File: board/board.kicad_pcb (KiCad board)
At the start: 4 copper layers, 21 x 13 mm, 4 parts, among them J1 0xx_LED, J2 0xx_LED

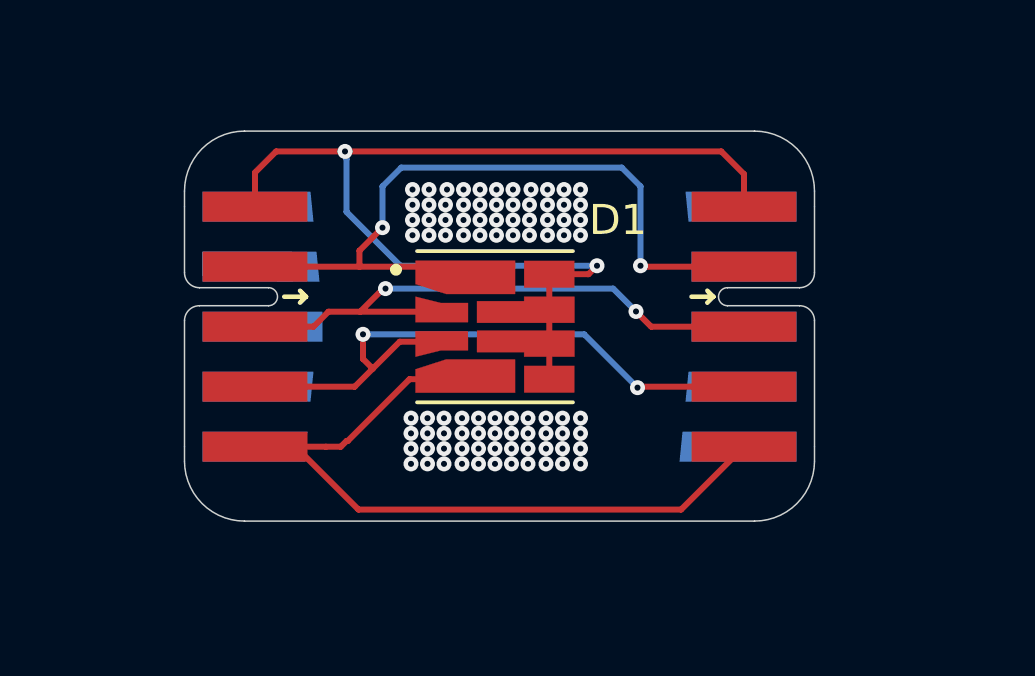
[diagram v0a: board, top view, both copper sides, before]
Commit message: Update surface and connected vias | Change common ground to common anode
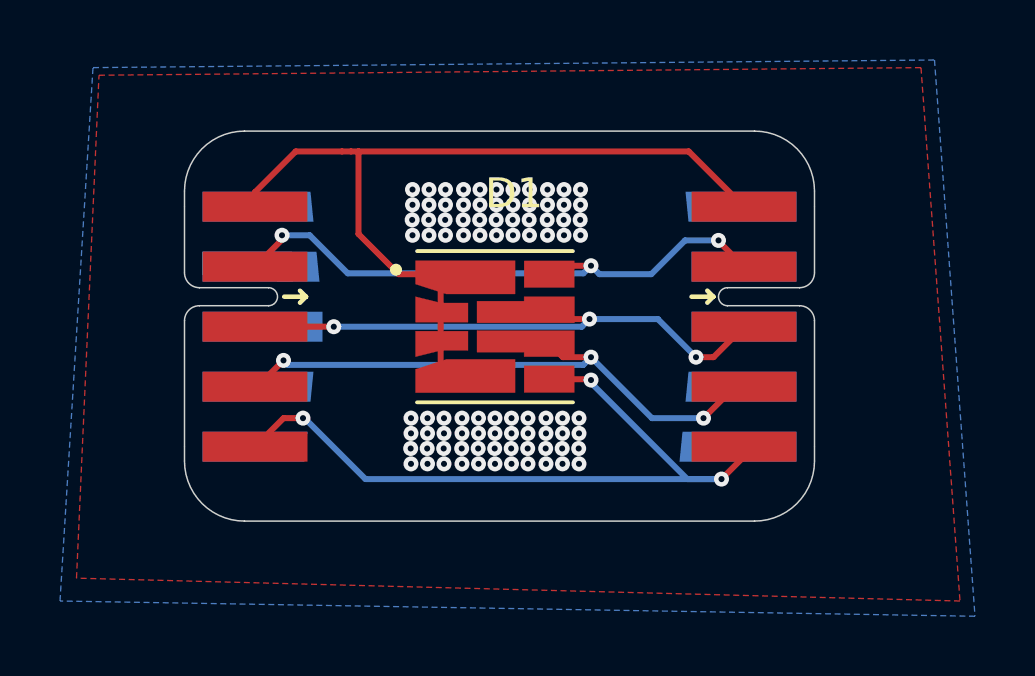
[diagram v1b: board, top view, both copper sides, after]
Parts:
- moved LOGO1 3.06 mm to (150.3, 96.0)
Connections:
- D1 pad 2: Net-(D1-Pad2) -> Net-(D1-Pad1)
- D1 pad 3: Net-(D1-Pad3) -> Net-(D1-Pad1)
- D1 pad 4: Net-(D1-Pad4) -> Net-(D1-Pad1)
- D1 pad 5: Net-(D1-Pad7) -> Net-(D1-Pad5)
- D1 pad 6: Net-(D1-Pad7) -> Net-(D1-Pad6)
- D1 pad 8: Net-(D1-Pad7) -> Net-(J2-Pad2)
- J1 pad 1: Net-(D1-Pad7) -> Net-(D1-Pad1)
- J1 pad 2: Net-(D1-Pad1) -> Net-(J2-Pad2)
- J1 pad 3: Net-(D1-Pad2) -> Net-(D1-Pad7)
- J1 pad 4: Net-(D1-Pad3) -> Net-(D1-Pad6)
- J1 pad 5: Net-(D1-Pad4) -> Net-(D1-Pad5)
- J2 pad 1: Net-(D1-Pad7) -> Net-(D1-Pad1)
- J2 pad 2: Net-(D1-Pad1) -> Net-(J2-Pad2)
- J2 pad 3: Net-(D1-Pad2) -> Net-(D1-Pad7)
- J2 pad 4: Net-(D1-Pad3) -> Net-(D1-Pad6)
- J2 pad 5: Net-(D1-Pad4) -> Net-(D1-Pad5)
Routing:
- net Net-(D1-Pad5): track 0.00 -> 25.4 mm, vias 0 -> 3
- net Net-(D1-Pad4): track 25.2 -> 0.00 mm
- net Net-(D1-Pad3): track 21.5 -> 0.00 mm, vias 2 -> 0
- net Net-(D1-Pad2): track 20.0 -> 0.00 mm, vias 2 -> 0
- net Net-(J2-Pad2): track 0.00 -> 19.9 mm, vias 0 -> 3
- net Net-(D1-Pad6): track 0.00 -> 19.7 mm, vias 0 -> 3
- net Net-(D1-Pad7): track 35.5 -> 18.8 mm, vias 2 -> 3
- net Net-(D1-Pad1): track 24.5 -> 28.0 mm, vias 2 -> 88
- net (no net): vias 88 -> 0
- added copper zone on B.Cu, net (none)
- added copper zone on F.Cu, net Net-(D1-Pad1)
- added copper zone on In1.Cu, net Net-(D1-Pad1)
- added copper zone on In2.Cu, net Net-(D1-Pad1)
- removed copper zone on In1.Cu, net (none)
- removed copper zone on In2.Cu, net (none)

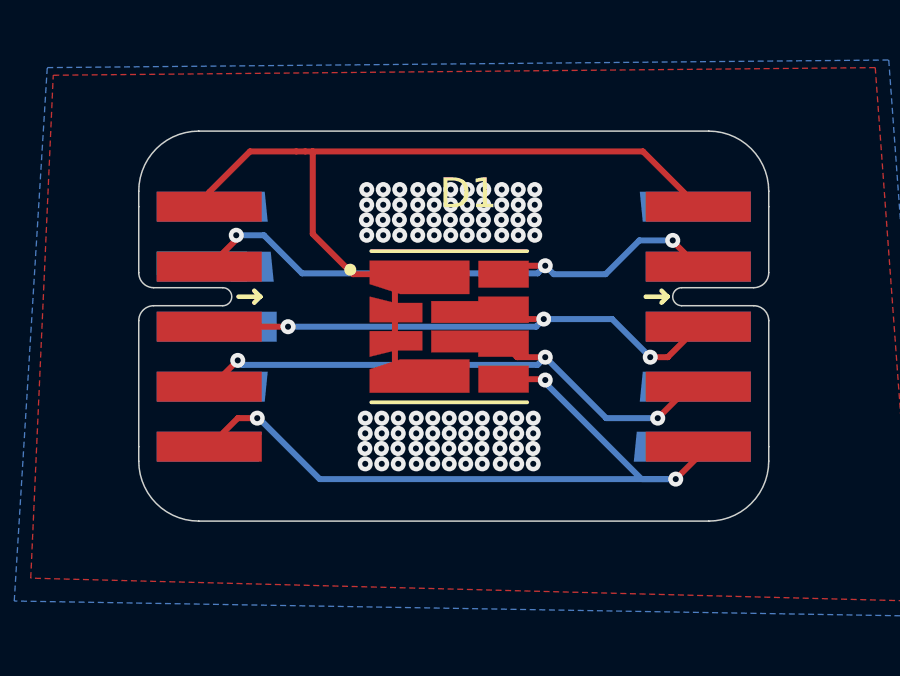
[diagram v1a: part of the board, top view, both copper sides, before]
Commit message: Update Layout | Remove DRC Errors | Connected unused Edgy Pins
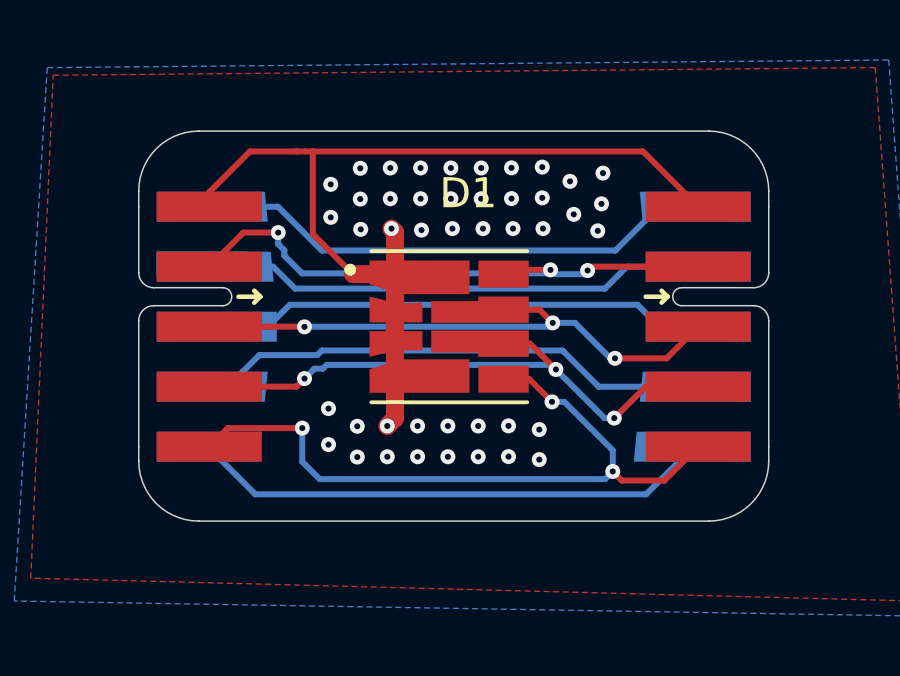
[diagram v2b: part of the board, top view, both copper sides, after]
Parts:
- J1, J2: value 0xx_LED -> 023_LED
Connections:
- J1 pad 10: (no net) -> Net-(J1-Pad10)
- J1 pad 6: (no net) -> Net-(J1-Pad6)
- J1 pad 7: (no net) -> Net-(J1-Pad7)
- J1 pad 8: (no net) -> Net-(J1-Pad8)
- J1 pad 9: (no net) -> Net-(J1-Pad9)
- J2 pad 10: (no net) -> Net-(J1-Pad10)
- J2 pad 6: (no net) -> Net-(J1-Pad6)
- J2 pad 7: (no net) -> Net-(J1-Pad7)
- J2 pad 8: (no net) -> Net-(J1-Pad8)
- J2 pad 9: (no net) -> Net-(J1-Pad9)
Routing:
- net Net-(J1-Pad10): track 0.00 -> 17.5 mm
- net Net-(J1-Pad6): track 0.00 -> 17.4 mm
- net Net-(J1-Pad9): track 0.00 -> 17.2 mm
- net Net-(J1-Pad7): track 0.00 -> 17.2 mm
- net Net-(J1-Pad8): track 0.00 -> 16.7 mm
- net Net-(D1-Pad1): track 28.0 -> 30.9 mm, vias 88 -> 44
- net Net-(D1-Pad5): track 25.4 -> 23.9 mm
- added copper zone on B.Cu, net Net-(D1-Pad1)
- removed copper zone on B.Cu, net (none)

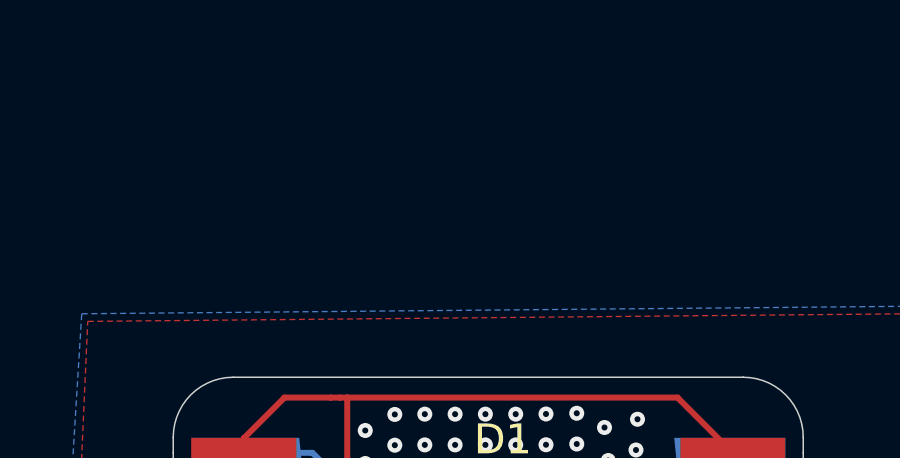
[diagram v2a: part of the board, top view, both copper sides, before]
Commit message: Change edgy connector back to GPIO | Began adding Resistor to specific voltage
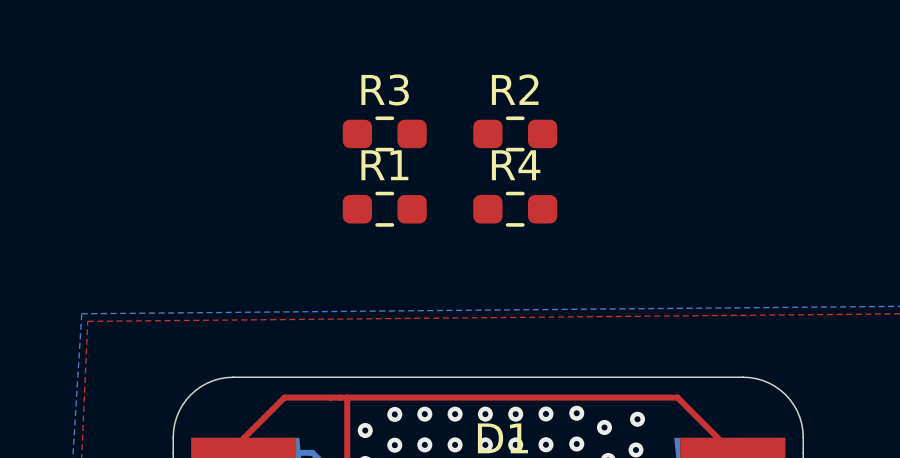
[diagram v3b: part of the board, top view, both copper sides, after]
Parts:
- added R1: R, Resistor_SMD:R_0603_1608Metric_Pad0.98x0.95mm_HandSolder, F.Cu at (147.1, 84.4)
- added R2: R, Resistor_SMD:R_0603_1608Metric_Pad0.98x0.95mm_HandSolder, F.Cu at (151.4, 81.9)
- added R3: R, Resistor_SMD:R_0603_1608Metric_Pad0.98x0.95mm_HandSolder, F.Cu at (147.1, 81.9)
- added R4: R, Resistor_SMD:R_0603_1608Metric_Pad0.98x0.95mm_HandSolder, F.Cu at (151.4, 84.4)
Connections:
- D1 pad 2: Net-(D1-Pad1) -> Net-(D1-Pad2)
- D1 pad 3: Net-(D1-Pad1) -> Net-(D1-Pad3)
- D1 pad 4: Net-(D1-Pad1) -> Net-(D1-Pad4)
- J1 pad 1: Net-(D1-Pad1) -> Net-(J1-Pad1)
- J2 pad 1: Net-(D1-Pad1) -> Net-(J1-Pad1)
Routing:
- net Net-(J1-Pad1): track 0.00 -> 30.9 mm
- net Net-(D1-Pad1): track 30.9 -> 0.00 mm

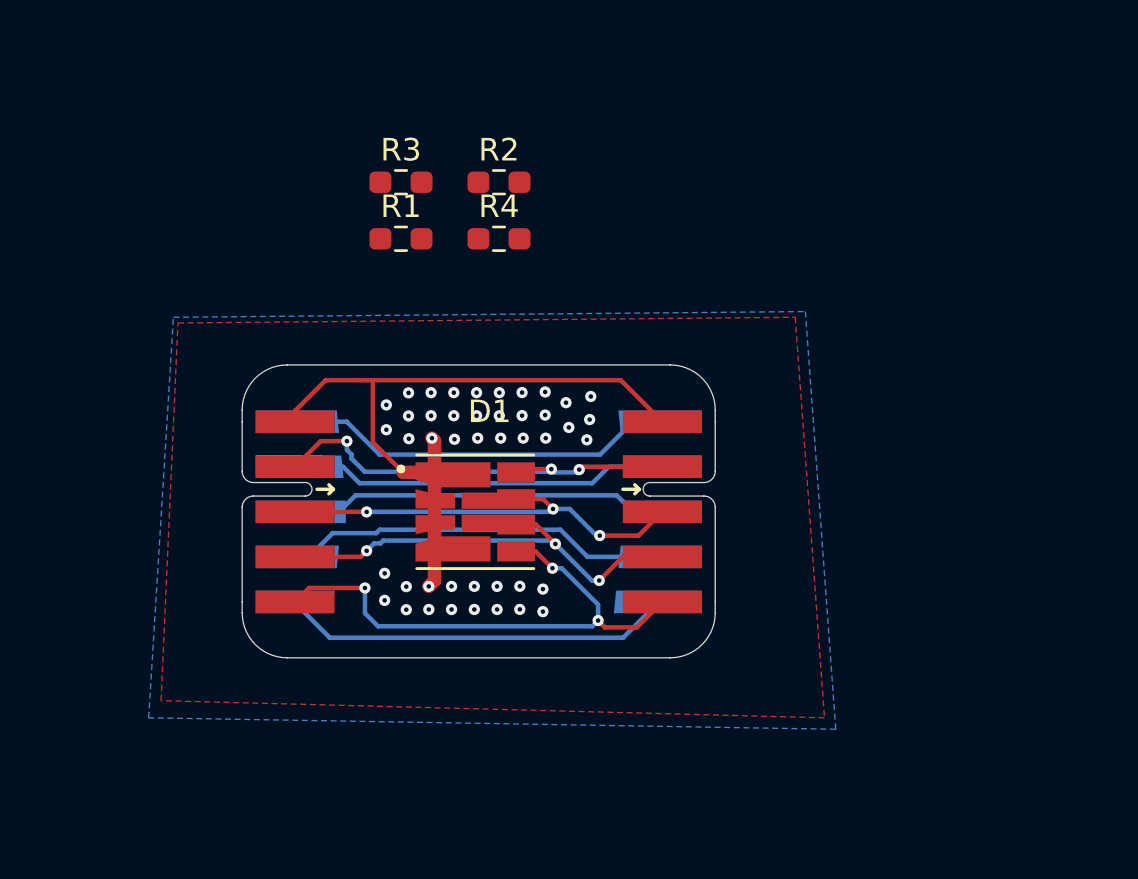
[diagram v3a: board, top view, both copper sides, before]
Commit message: Increase PCB size | Update Design
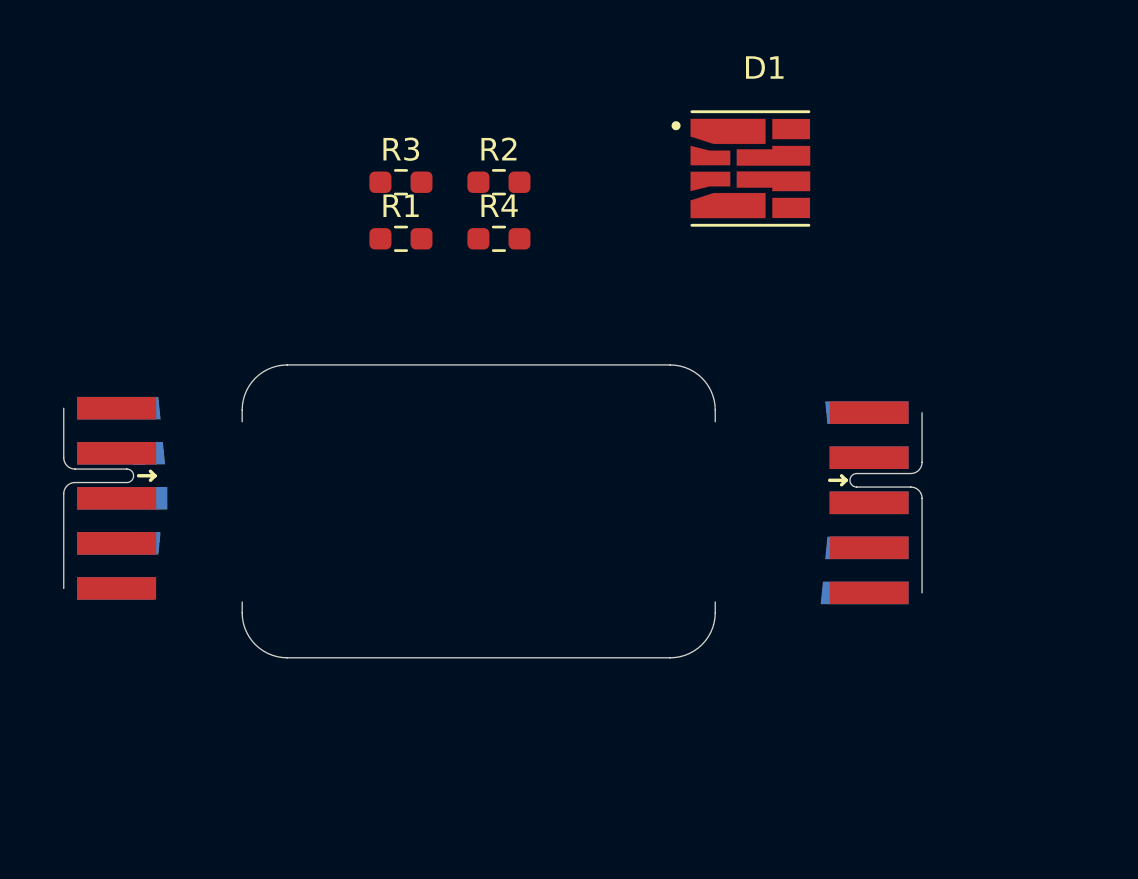
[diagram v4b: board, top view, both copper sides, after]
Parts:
- moved D1 19.5 mm to (162.6, 81.3)
- moved LOGO1 13.5 mm to (147.3, 109.2)
- moved J2 9.19 mm to (170.2, 96.1)
- moved J1 7.94 mm to (132.1, 95.9)
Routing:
- net Net-(J1-Pad1): track 30.9 -> 0.00 mm
- net Net-(D1-Pad5): track 23.9 -> 0.00 mm, vias 3 -> 0
- net Net-(D1-Pad6): track 19.9 -> 0.00 mm, vias 3 -> 0
- net Net-(D1-Pad8): track 19.5 -> 0.00 mm, vias 3 -> 0
- net Net-(D1-Pad7): track 19.1 -> 0.00 mm, vias 3 -> 0
- net Net-(J1-Pad10): track 17.5 -> 0.00 mm
- net Net-(J1-Pad6): track 17.4 -> 0.00 mm
- net Net-(J1-Pad9): track 17.2 -> 0.00 mm
- net Net-(J1-Pad7): track 17.2 -> 0.00 mm
- net Net-(J1-Pad8): track 16.7 -> 0.00 mm
- net Net-(D1-Pad1): vias 44 -> 0
- removed copper zone on B.Cu, net Net-(D1-Pad1)
- removed copper zone on F.Cu, net Net-(D1-Pad1)
- removed copper zone on In1.Cu, net Net-(D1-Pad1)
- removed copper zone on In2.Cu, net Net-(D1-Pad1)

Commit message: Add value to resistor
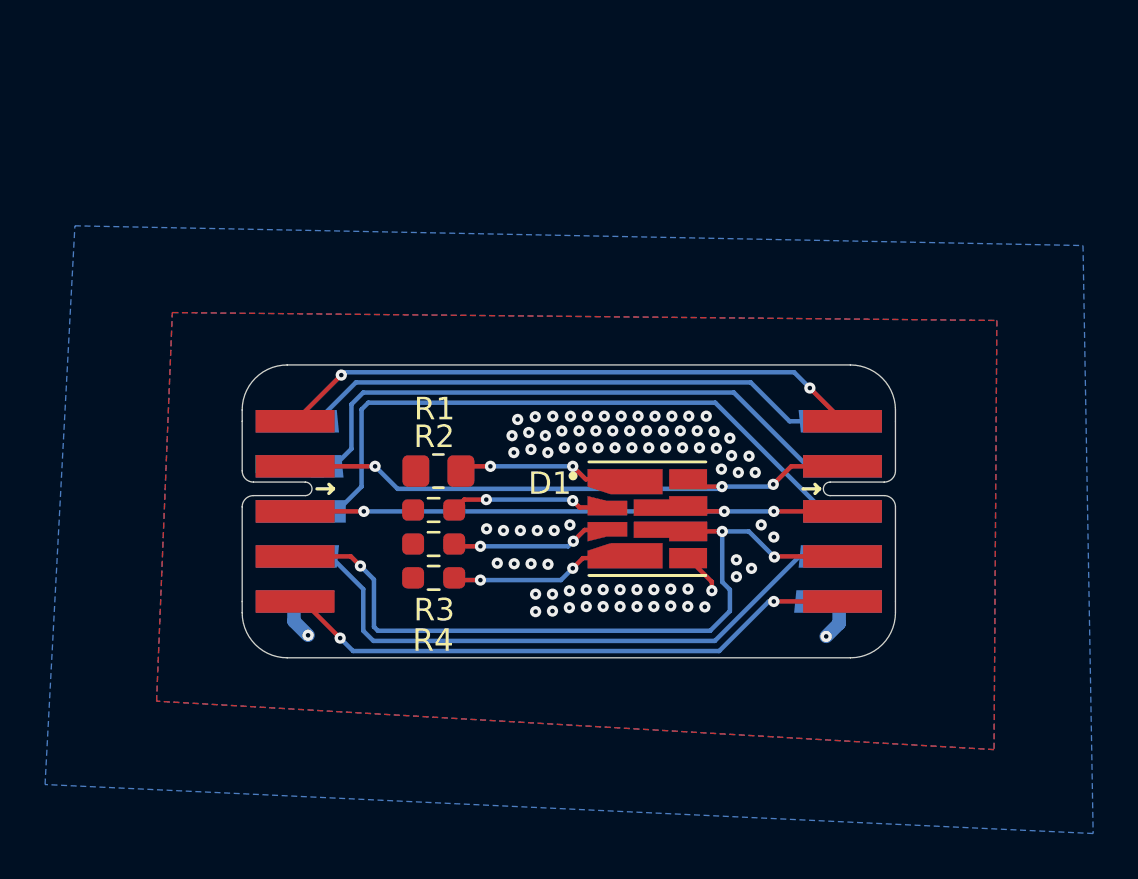
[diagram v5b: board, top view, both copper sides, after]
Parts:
- R1: value R -> 11,5R; footprint Resistor_SMD:R_0603_1608Metric_Pad0.98x0.95mm_HandSolder -> Resistor_SMD:R_0805_2012Metric_Pad1.20x1.40mm_HandSolder
- R2, R3: value R -> 6,6R
- R4: value R -> 6R
- moved LOGO1 18.3 mm to (132.5, 120.0)
- moved D1 16.2 mm to (158.0, 96.8)
- moved R3 16.1 mm to (148.5, 98.0)
- moved R4 15.3 mm to (148.5, 99.5)
- moved R2 14.8 mm to (148.5, 96.4)
- moved R1 10.4 mm to (148.7, 94.7)
- moved J1 7.94 mm to (140.0, 96.5)
- moved J2 1.24 mm to (169.0, 96.5)
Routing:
- net Net-(D1-Pad6): track 0.00 -> 33.3 mm, vias 0 -> 3
- net Net-(D1-Pad5): track 0.00 -> 31.0 mm, vias 0 -> 3
- net Net-(J1-Pad8): track 0.00 -> 30.1 mm
- net Net-(J1-Pad7): track 0.00 -> 28.4 mm
- net Net-(J1-Pad9): track 0.00 -> 28.4 mm
- net Net-(D1-Pad8): track 0.00 -> 26.8 mm, vias 0 -> 3
- net Net-(J1-Pad1): track 0.00 -> 26.1 mm, vias 0 -> 2
- net Net-(D1-Pad7): track 0.00 -> 26.0 mm, vias 0 -> 3
- net Net-(J1-Pad6): track 0.00 -> 25.6 mm
- net Net-(D1-Pad1): track 0.00 -> 7.21 mm, vias 0 -> 2
- net Net-(D1-Pad4): track 0.00 -> 7.21 mm, vias 0 -> 2
- net Net-(D1-Pad2): track 0.00 -> 7.13 mm, vias 0 -> 2
- net Net-(D1-Pad3): track 0.00 -> 7.11 mm, vias 0 -> 2
- net Net-(J1-Pad10): track 0.00 -> 3.55 mm, vias 0 -> 81
- net (no net): vias 0 -> 1
- added copper zone on B.Cu, net Net-(J1-Pad10)
- added copper zone on F.Cu, net Net-(J1-Pad10)
- added copper zone on In1.Cu, net Net-(J1-Pad10)
- added copper zone on In2.Cu, net Net-(J1-Pad10)
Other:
- board size 21 x 13 mm -> 29 x 13 mm
